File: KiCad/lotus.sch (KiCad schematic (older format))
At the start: 32 parts, among them IC1 DW01A-G, J1 USB_OTG, Q1 FS8205A, SW1 SW_Push, SW2 SW_DIP_x01, U1 LD1117S33CTR, U2 TP4056, U3 ESP-12E

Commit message: Adicionado footprints
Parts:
- C1, C2, C3, C4: footprint (none) -> Capacitors_SMD:C_0402
- C5: renamed from C?; footprint (none) -> Capacitors_SMD:C_0402
- C6, C7: renamed from C?; footprint (none) -> Capacitors_Tantalum_SMD:CP_Tantalum_Case-C_EIA-6032-28_Hand
- D1: footprint (none) -> LEDs:LED_D5.0mm-4
- IC1: footprint SOT95P190X145-6N -> DW01A-G:SOT95P190X145-6N
- J1: footprint (none) -> Connectors:USB_Micro-B
- J2: renamed from J?; footprint (none) -> Pin_Headers:Pin_Header_Straight_1x04_Pitch2.54mm
- Q1: footprint SOP65P640X120-8N -> FS8205A:SOP65P640X120-8N
- R1, R10, R11, R2, R3, R5, R6, R7, R8, R9: footprint (none) -> Resistors_SMD:R_0402
- R12, R13, R4: renamed from R?; footprint (none) -> Resistors_SMD:R_0402
- SW1: footprint (none) -> Buttons_Switches_THT:SW_PUSH_6mm
- SW2: footprint (none) -> Buttons_Switches_SMD:SW_DIP_x1_W5.08mm_Slide_Copal_CHS-A
- SW3: renamed from SW?; footprint (none) -> Buttons_Switches_THT:SW_PUSH_6mm
- U3: footprint (none) -> RF_Modules:ESP-12E

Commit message: Terminado definição dos footprints
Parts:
- BT1: footprint (none) -> Pin_Headers:Pin_Header_Straight_1x02_Pitch2.54mm
- SW2: symbol SW_DIP_x01 -> SW_DIP_x01-RESCUE-lotus
- U2: footprint (none) -> TP4056:TP4056; symbol TP4056 -> TP4056-RESCUE-lotus
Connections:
- net GND: no longer U2.PAD
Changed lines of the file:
@@
 EESchema Schematic File Version 2
+LIBS:lotus-rescue
 LIBS:power
 LIBS:device
@@
 $EndComp
 $Comp
-L TP4056 U2
+L TP4056-RESCUE-lotus U2
 U 1 1 5AE4FD92
 P 5100 1950
 F 0 "U2" H 4750 2350 60  0000 L CNN
 F 1 "TP4056" H 5450 2350 60  0000 R CNN
-F 2 "" H 5100 1950 60  0001 C CNN
+F 2 "TP4056:TP4056" H 5100 1950 60  0001 C CNN
 F 3 "" H 5100 1950 60  0000 C CNN
 	1    5100 1950
@@
 $EndComp
 $Comp
-L SW_DIP_x01 SW2
+L SW_DIP_x01-RESCUE-lotus SW2
 U 1 1 5AE54D5B
 P 10400 4600
@@
 F 0 "BT1" H 8850 2350 50  0000 L CNN
 F 1 "Battery_Cell" H 8850 2250 50  0000 L CNN
-F 2 "" V 8750 2310 50  0001 C CNN
+F 2 "Pin_Headers:Pin_Header_Straight_1x02_Pitch2.54mm" V 8750 2310 50  0001 C CNN
 F 3 "" V 8750 2310 50  0001 C CNN
 	1    8750 2250
@@
 L GND #PWR03
 U 1 1 5AEA0B83
-P 5100 2450
-F 0 "#PWR03" H 5100 2200 50  0001 C CNN
-F 1 "GND" H 5100 2300 50  0000 C CNN
-F 2 "" H 5100 2450 50  0001 C CNN
-F 3 "" H 5100 2450 50  0001 C CNN
-	1    5100 2450
+P 5100 2390
+F 0 "#PWR03" H 5100 2140 50  0001 C CNN
+F 1 "GND" H 5100 2240 50  0000 C CNN
+F 2 "" H 5100 2390 50  0001 C CNN
+F 3 "" H 5100 2390 50  0001 C CNN
+	1    5100 2390
 	1    0    0    -1
 $EndComp
@@
 	5600 2000 5850 2000
 Wire Wire Line
-	4600 1700 4600 1750
-Wire Wire Line
-	4600 1750 4600 1800
-Wire Wire Line
-	9900 3000 8400 3000
-Wire Wire Line
-	8400 3000 6150 3000
-Wire Wire Line
-	6150 3000 5700 3000
-Wire Wire Line
-	5700 3000 4200 3000
-Wire Wire Line
-	4200 3000 3650 3000
-Wire Wire Line
-	3650 3000 3000 3000
+	4600 1700 4600 1800
+Wire Wire Line
+	9900 3000 3000 3000
 Wire Wire Line
 	5700 3000 5700 2650
@@
 	4200 3000 4200 2900
 Wire Wire Line
-	4200 1750 4200 2400
-Wire Wire Line
-	4200 2400 4200 2600
+	4200 1750 4200 2600
 Wire Wire Line
 	4200 1750 4600 1750
@@
 Connection ~ 4200 3000
 Wire Wire Line
-	6250 2550 6250 2600
-Wire Wire Line
-	6250 2600 6250 2650
-Wire Wire Line
-	7550 2550 7550 2600
-Wire Wire Line
-	7550 2600 7550 2650
+	6250 2550 6250 2650
+Wire Wire Line
+	7550 2550 7550 2650
 Wire Wire Line
 	6250 2600 6150 2600
 Wire Wire Line
-	6150 2100 6150 2600
-Wire Wire Line
-	6150 2600 6150 3000
+	6150 2100 6150 3000
 Connection ~ 6250 2600
 Wire Wire Line
@@
 	6350 1750 6350 1400
 Wire Wire Line
-	7550 1600 7750 1600
-Wire Wire Line
-	7750 1600 8050 1600
+	7550 1600 8050 1600
 Wire Wire Line
 	7550 1600 7550 1500
@@
 	7550 1500 7350 1500
 Wire Wire Line
-	7550 1300 7600 1300
-Wire Wire Line
-	7600 1300 7750 1300
+	7550 1300 7750 1300
 Wire Wire Line
 	7550 1300 7550 1400
@@
 	7600 1300 7600 2600
 Wire Wire Line
-	7550 2600 7600 2600
-Wire Wire Line
-	7600 2600 8750 2600
+	7550 2600 8750 2600
 Connection ~ 7550 2600
 Connection ~ 7600 1300
@@
 Connection ~ 7750 1600
 Wire Wire Line
-	8400 1100 8400 1600
-Wire Wire Line
-	8400 1600 8400 2100
-Wire Wire Line
-	8350 1600 8400 1600
-Wire Wire Line
-	8400 1600 8750 1600
+	8400 1100 8400 2100
+Wire Wire Line
+	8350 1600 8750 1600
 Wire Wire Line
 	8400 3000 8400 2400
@@
 Connection ~ 8400 1600
 Wire Wire Line
-	5600 1100 8400 1100
-Wire Wire Line
-	8400 1100 9300 1100
-Wire Wire Line
-	9300 1100 9500 1100
+	5600 1100 9500 1100
 Wire Wire Line
 	5600 1100 5600 1700
@@
 	6300 4900 6800 4900
 Wire Wire Line
-	4050 4650 4250 4650
-Wire Wire Line
-	4250 4650 4450 4650
+	4050 4650 4450 4650
 Wire Wire Line
 	4250 4650 4250 4700
 Connection ~ 4250 4650
 Wire Wire Line
-	4050 4100 4250 4100
-Wire Wire Line
-	4250 4100 4450 4100
+	4050 4100 4450 4100
 Wire Wire Line
 	4550 2200 4600 2200
@@
 	5850 2000 5850 2050
 Wire Wire Line
-	5100 2350 5100 2450
-Wire Wire Line
-	5100 2450 5150 2450
-Wire Wire Line
-	5150 2450 5150 2350
+	5100 2350 5100 2390
 Wire Wire Line
 	8750 4900 8600 4900
@@
 	10850 4600 10850 4650
 Wire Wire Line
-	8600 4600 10000 4600
-Wire Wire Line
-	10000 4600 10100 4600
+	8600 4600 10100 4600
 Wire Wire Line
 	10000 4250 10000 4600
@@
 	10700 4600 10850 4600
 Wire Wire Line
-	8600 4500 9200 4500
-Wire Wire Line
-	9200 4500 9300 4500
-Wire Wire Line
-	8600 4400 9000 4400
-Wire Wire Line
-	9000 4400 9300 4400
+	8600 4500 9300 4500
+Wire Wire Line
+	8600 4400 9300 4400
 Wire Wire Line
 	9200 4500 9200 4150
@@
 Connection ~ 8400 1100
 Wire Wire Line
-	9900 1400 9900 1800
-Wire Wire Line
-	9900 1800 9900 3000
+	9900 1400 9900 3000
 Wire Wire Line
 	5900 4400 5900 4200
 Wire Wire Line
-	10300 1100 10500 1100
-Wire Wire Line
-	10500 1100 10700 1100
+	10300 1100 10700 1100
 Wire Wire Line
 	4250 3650 4250 3600
@@
 	9300 1650 9300 1800
 Wire Wire Line
-	9300 1800 9900 1800
-Wire Wire Line
-	9900 1800 10500 1800
+	9300 1800 10500 1800
 Connection ~ 9900 1800
 Wire Wire Line
@@
 	4850 5750 4350 5750
 Wire Wire Line
-	4250 3950 4250 4000
-Wire Wire Line
-	4250 4000 4250 4100
+	4250 3950 4250 4100
 Connection ~ 4250 4100
 Wire Wire Line
@@
 Connection ~ 4250 4000
 Wire Wire Line
-	2700 4650 2900 4650
-Wire Wire Line
-	2900 4650 3100 4650
+	2700 4650 3100 4650
 Wire Wire Line
 	2900 4650 2900 4700
 Connection ~ 2900 4650
 Wire Wire Line
-	2700 4100 2900 4100
-Wire Wire Line
-	2900 4100 3100 4100
+	2700 4100 3100 4100
 Wire Wire Line
 	2900 3650 2900 3600
 Wire Wire Line
-	2900 3950 2900 4000
-Wire Wire Line
-	2900 4000 2900 4100
+	2900 3950 2900 4100
 Connection ~ 2900 4100
 Wire Wire Line
@@
 	6800 4400 5900 4400
 Wire Wire Line
-	3300 2400 3650 2400
-Wire Wire Line
-	3650 2400 4200 2400
+	3300 2400 4200 2400
 Connection ~ 4200 2400
 Wire Wire Line

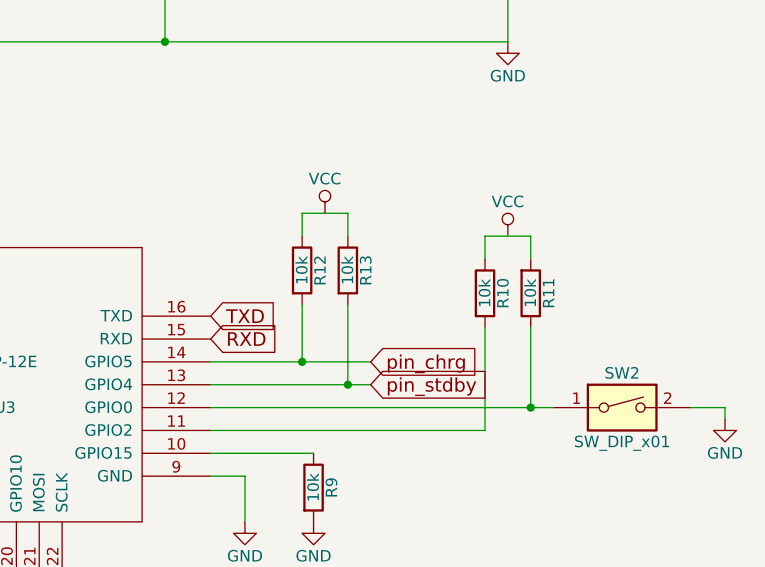
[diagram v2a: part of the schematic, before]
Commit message: Organizado footprints no PCB
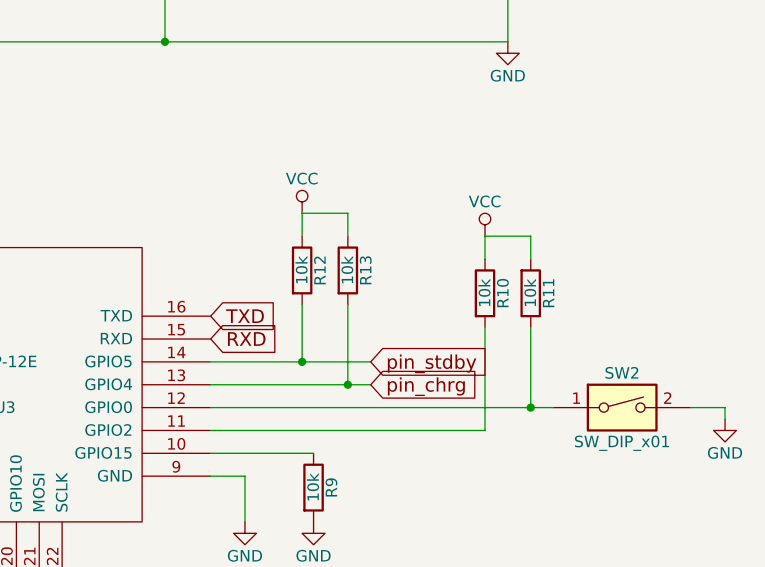
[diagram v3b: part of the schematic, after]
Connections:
- net VCC: now also R10.1, R11.2, R12.1, R13.1
- net pin_chrg: now also R13.2, U3.13 (GPIO4); no longer R12.2, U3.14 (GPIO5)
- net pin_stdby: now also R12.2, U3.14 (GPIO5); no longer R13.2, U3.13 (GPIO4)
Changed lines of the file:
@@
 Text GLabel 3950 2200 0    60   Input ~ 0
 pin_stdby
+Text GLabel 9300 4400 2    60   Input ~ 0
+pin_stdby
 Text GLabel 9300 4500 2    60   Input ~ 0
-pin_stdby
-Text GLabel 9300 4400 2    60   Input ~ 0
 pin_chrg
 $Comp
@@
 L VCC #PWR07
 U 1 1 5AEA21C3
-P 9900 3850
-F 0 "#PWR07" H 9900 3700 50  0001 C CNN
-F 1 "VCC" H 9900 4000 50  0000 C CNN
-F 2 "" H 9900 3850 50  0001 C CNN
-F 3 "" H 9900 3850 50  0001 C CNN
-	1    9900 3850
+P 9800 3850
+F 0 "#PWR07" H 9800 3700 50  0001 C CNN
+F 1 "VCC" H 9800 4000 50  0000 C CNN
+F 2 "" H 9800 3850 50  0001 C CNN
+F 3 "" H 9800 3850 50  0001 C CNN
+	1    9800 3850
 	1    0    0    -1
 $EndComp
@@
 L VCC #PWR018
 U 1 1 5AEB2D49
-P 9100 3750
-F 0 "#PWR018" H 9100 3600 50  0001 C CNN
-F 1 "VCC" H 9100 3900 50  0000 C CNN
-F 2 "" H 9100 3750 50  0001 C CNN
-F 3 "" H 9100 3750 50  0001 C CNN
-	1    9100 3750
-	1    0    0    -1
-$EndComp
+P 9000 3750
+F 0 "#PWR018" H 9000 3600 50  0001 C CNN
+F 1 "VCC" H 9000 3900 50  0000 C CNN
+F 2 "" H 9000 3750 50  0001 C CNN
+F 3 "" H 9000 3750 50  0001 C CNN
+	1    9000 3750
+	1    0    0    -1
+$EndComp
